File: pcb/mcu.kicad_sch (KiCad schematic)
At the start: 15 parts

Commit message: everything except crystal
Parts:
- added J?: Conn_02x07_Top_Bottom, symbol Connector_Generic:Conn_02x07_Top_Bottom
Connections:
- net +3.3V: now also J?.13 (Pin_13); no longer U?.G3 (VSS)
- net DONE: now also U?.D10 (PC8); no longer U?.E2 (PA5)
- net GND: now also U?.G3 (VSS), J?.14 (Pin_14)
- net PROGRAM_B: now also U?.D9 (PE7); no longer U?.E1 (PA6)
- net MCU_GPIO_1: now reaches U?.C1 (PA1)
- net MCU_GPIO_1: now also J?.1 (Pin_1)
- net MCU_GPIO_2: now reaches U?.C2 (PA0)
- net MCU_GPIO_2: now also J?.2 (Pin_2)
- net MCU_GPIO_3: now reaches U?.C3 (PE10)
- net MCU_GPIO_3: now also J?.3 (Pin_3)
- net MCU_GPIO_4: now reaches U?.C4 (PD13)
- net MCU_GPIO_4: now also J?.4 (Pin_4)
- net MCU_GPIO_5: now reaches U?.C5 (PD12)
- net MCU_GPIO_5: now also J?.5 (Pin_5)
- net MCU_GPIO_6: now reaches U?.C6 (PF9)
- net MCU_GPIO_6: now also J?.6 (Pin_6)
- net MCU_GPIO_12: now reaches U?.E10 (PE1)
- net MCU_GPIO_12: now also J?.12 (Pin_12)
- net MCU_GPIO_9: now reaches U?.E3 (PA4)
- net MCU_GPIO_9: now also J?.9 (Pin_9)
- net MCU_GPIO_10: now reaches U?.E4 (PB0)
- net MCU_GPIO_10: now also J?.10 (Pin_10)
- net MCU_GPIO_11: now reaches U?.E9 (PE0)
- net MCU_GPIO_11: now also J?.11 (Pin_11)
- new net MCU_GPIO_7: J?.7 (Pin_7), U?.E1 (PA6)
- new net MCU_GPIO_8: J?.8 (Pin_8), U?.E2 (PA5)
- no-connect marks 55 -> 43
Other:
- note added: "MCU PGIO HEADER"
- note added: "MCU clock out"
- moved on the sheet: C?

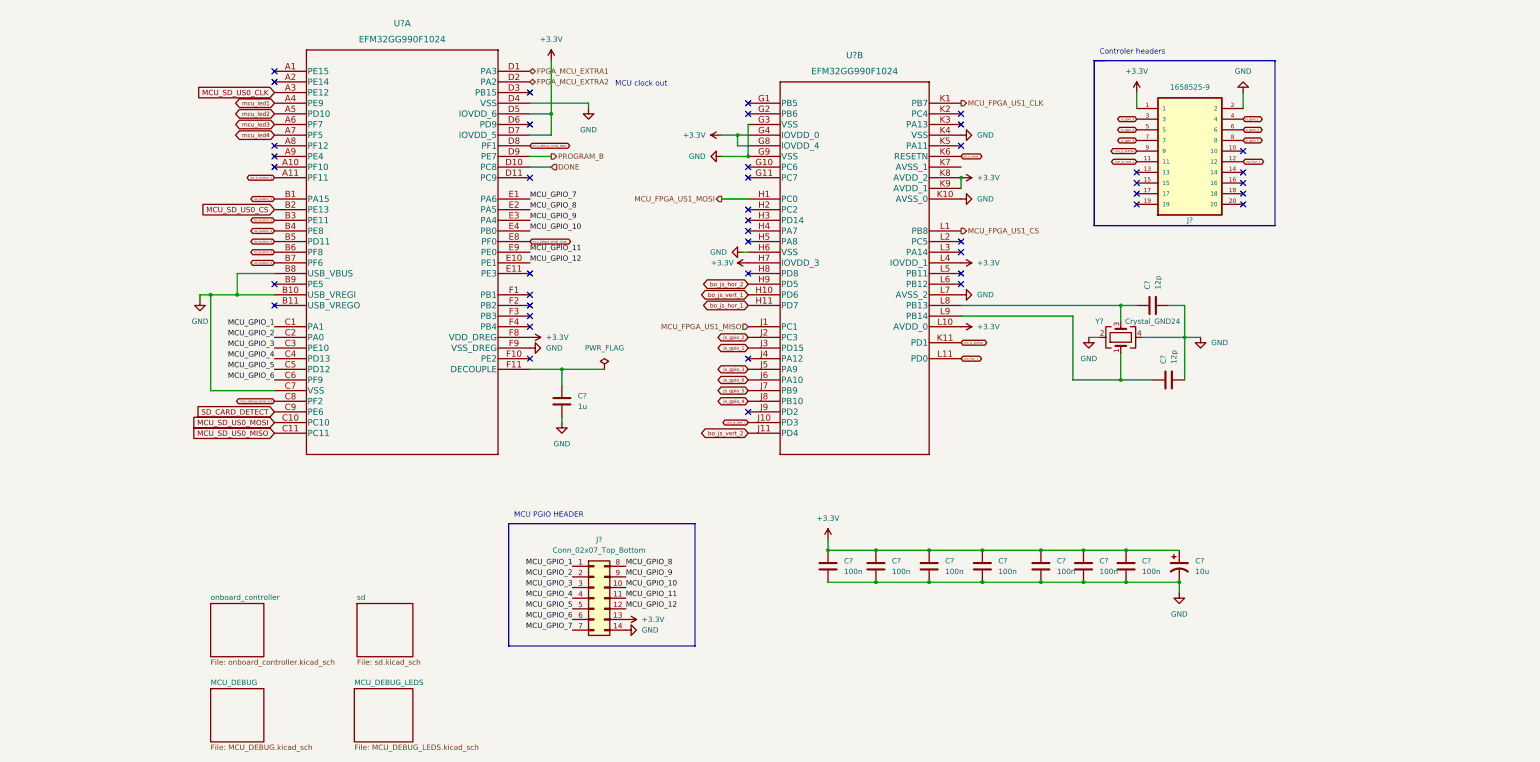
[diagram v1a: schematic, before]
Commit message: add oscilattor + spi debug+ cap on sramd
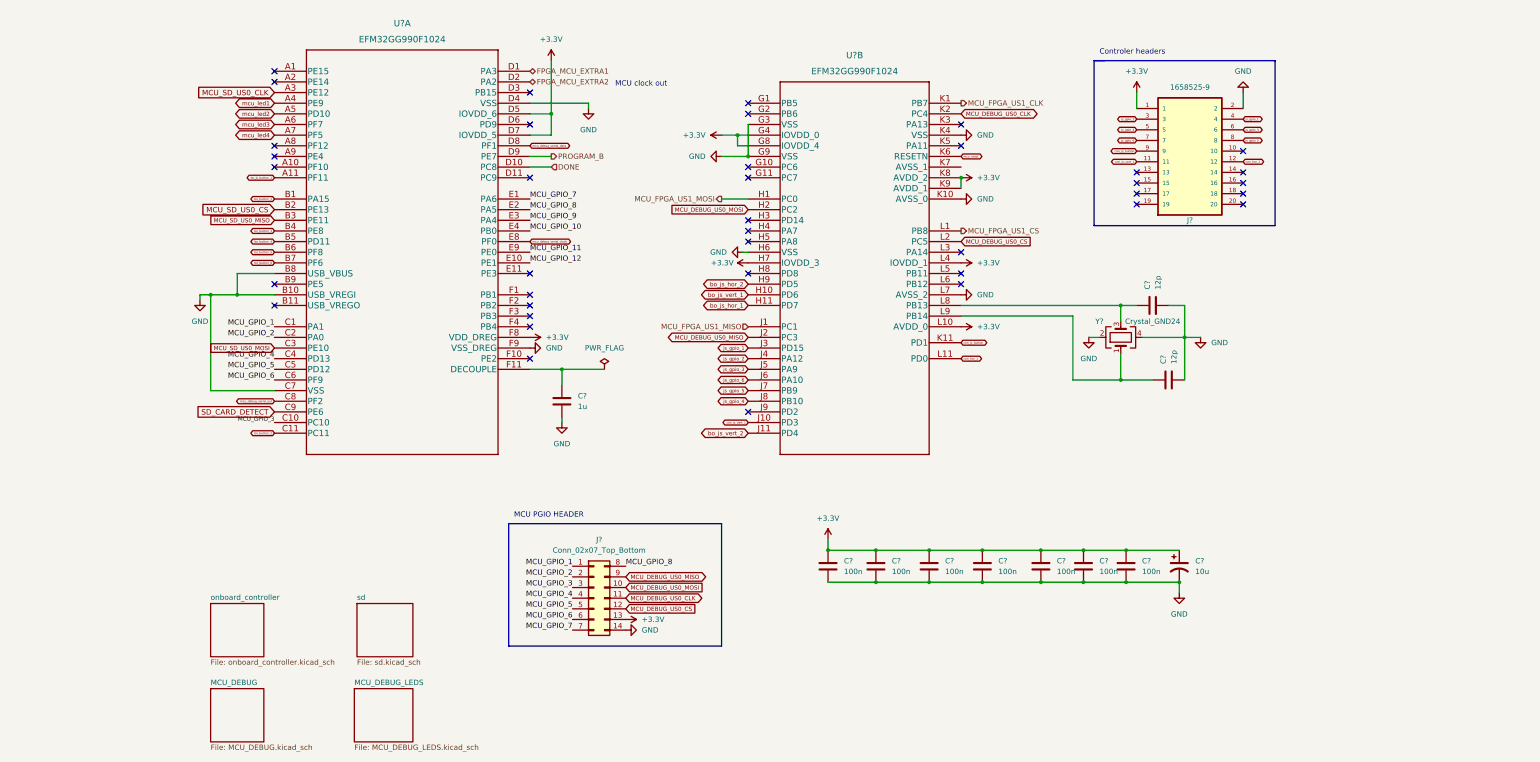
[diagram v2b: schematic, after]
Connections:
- net MCU_GPIO_10: no longer J?.10 (Pin_10)
- net MCU_GPIO_11: no longer J?.11 (Pin_11)
- net MCU_GPIO_12: no longer J?.12 (Pin_12)
- net MCU_GPIO_3: now also U?.C10 (PC10); no longer U?.C3 (PE10)
- net MCU_GPIO_9: no longer J?.9 (Pin_9)
- net MCU_SD_US0_MISO: now also U?.B3 (PE11); no longer U?.C11 (PC11)
- net MCU_SD_US0_MOSI: now also U?.C3 (PE10); no longer U?.C10 (PC10)
- net bo_button_2: now also U?.C11 (PC11); no longer U?.B3 (PE11)
- net js_gpio_2: now also U?.J4 (PA12); no longer U?.J2 (PC3)
- net MCU_DEBUG_US0_MOSI: now reaches U?.H2 (PC2)
- net MCU_DEBUG_US0_MOSI: now also J?.10 (Pin_10)
- net MCU_DEBUG_US0_CLK: now reaches U?.K2 (PC4)
- net MCU_DEBUG_US0_CLK: now also J?.11 (Pin_11)
- net MCU_DEBUG_US0_CS: now reaches U?.L2 (PC5)
- net MCU_DEBUG_US0_CS: now also J?.12 (Pin_12)
- new net MCU_DEBUG_US0_MISO: J?.9 (Pin_9), U?.J2 (PC3)
- no-connect marks 43 -> 39
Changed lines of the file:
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@@
   (no_connect (at 34.29 52.07))
   (no_connect (at 34.29 29.21))
-  (no_connect (at 147.32 62.23))
   (no_connect (at 198.12 72.39))
   (no_connect (at 95.25 97.79))
@@
   (no_connect (at 95.25 54.61))
   (no_connect (at 95.25 41.91))
-  (no_connect (at 147.32 97.79))
   (no_connect (at 147.32 64.77))
   (no_connect (at 147.32 77.47))
@@
   (no_connect (at 198.12 80.01))
   (no_connect (at 34.29 80.01))
-  (no_connect (at 198.12 39.37))
   (no_connect (at 198.12 41.91))
-  (no_connect (at 198.12 69.85))
   (no_connect (at 95.25 77.47))
   (no_connect (at 34.29 46.99))
@@
     (stroke (width 0) (type default) (color 0 0 0 0))
   )
-  (polyline (pts (xy 134.62 137.16) (xy 134.62 166.37))
-    (stroke (width 0) (type default) (color 0 0 0 0))
-  )
   (wire (pts (xy 236.22 102.87) (xy 243.84 102.87))
     (stroke (width 0) (type default) (color 0 0 0 0))
@@
     (stroke (width 0) (type default) (color 0 0 0 0))
   )
-  (polyline (pts (xy 134.62 166.37) (xy 90.17 166.37))
+  (polyline (pts (xy 134.62 137.16) (xy 140.97 137.16))
+    (stroke (width 0) (type default) (color 0 0 0 0))
+  )
+  (polyline (pts (xy 140.97 166.37) (xy 90.17 166.37))
     (stroke (width 0) (type default) (color 0 0 0 0))
   )
@@
     (stroke (width 0) (type default) (color 0 0 0 0))
   )
+  (polyline (pts (xy 140.97 137.16) (xy 140.97 166.37))
+    (stroke (width 0) (type default) (color 0 0 0 0))
+  )
   (wire (pts (xy 95.25 100.33) (xy 102.87 100.33))
     (stroke (width 0) (type default) (color 0 0 0 0))
@@
     (effects (font (size 1.27 1.27)) (justify right bottom))
   )
-  (label "MCU_GPIO_11" (at 118.11 154.94 0)
-    (effects (font (size 1.27 1.27)) (justify left bottom))
-  )
   (label "MCU_GPIO_5" (at 34.29 100.33 180)
     (effects (font (size 1.27 1.27)) (justify right bottom))
   )
-  (label "MCU_GPIO_3" (at 34.29 95.25 180)
-    (effects (font (size 1.27 1.27)) (justify right bottom))
+  (label "MCU_GPIO_3" (at 34.29 113.03 180)
+    (effects (font (size 1 1)) (justify right bottom))
   )
   (label "MCU_GPIO_6" (at 105.41 160.02 180)
@@
     (effects (font (size 1.27 1.27)) (justify right bottom))
   )
-  (label "MCU_GPIO_10" (at 118.11 152.4 0)
-    (effects (font (size 1.27 1.27)) (justify left bottom))
-  )
   (label "MCU_GPIO_6" (at 34.29 102.87 180)
     (effects (font (size 1.27 1.27)) (justify right bottom))
@@
     (effects (font (size 1.27 1.27)) (justify right bottom))
   )
-  (label "MCU_GPIO_12" (at 118.11 157.48 0)
-    (effects (font (size 1.27 1.27)) (justify left bottom))
-  )
   (label "MCU_GPIO_7" (at 105.41 162.56 180)
     (effects (font (size 1.27 1.27)) (justify right bottom))
@@
     (effects (font (size 1.27 1.27)) (justify left bottom))
   )
-  (label "MCU_GPIO_9" (at 118.11 149.86 0)
-    (effects (font (size 1.27 1.27)) (justify left bottom))
-  )
   (label "MCU_GPIO_1" (at 34.29 90.17 180)
     (effects (font (size 1.27 1.27)) (justify right bottom))
@@
   (label "MCU_GPIO_8" (at 118.11 147.32 0)
     (effects (font (size 1.27 1.27)) (justify left bottom))
+  )
+  (global_label "MCU_DEBUG_US0_CS" (shape input) (at 118.11 157.48 0) (fields_autoplaced)
+    (effects (font (size 1 1)) (justify left))
+    (property "Intersheet References" "${INTERSHEET_REFS}" (id 0) (at 135.3433 157.4175 0)
+      (effects (font (size 1 1)) (justify left) hide)
+    )
   )
   (global_label "mcu_led1" (shape bidirectional) (at 34.29 36.83 180) (fields_autoplaced)
@@
     )
   )
+  (global_label "MCU_DEBUG_US0_MOSI" (shape input) (at 118.11 152.4 0) (fields_autoplaced)
+    (effects (font (size 1 1)) (justify left))
+    (property "Intersheet References" "${INTERSHEET_REFS}" (id 0) (at 137.01 152.4625 0)
+      (effects (font (size 1 1)) (justify left) hide)
+    )
+  )
   (global_label "MCU_SD_US0_CLK" (shape input) (at 34.29 34.29 180) (fields_autoplaced)
     (effects (font (size 1.27 1.27)) (justify right))
@@
     )
   )
+  (global_label "js_gpio_2" (shape bidirectional) (at 147.32 97.79 180) (fields_autoplaced)
+    (effects (font (size 0.8 0.8)) (justify right))
+    (property "Intersheet References" "${INTERSHEET_REFS}" (id 0) (at 140.2381 97.74 0)
+      (effects (font (size 0.8 0.8)) (justify right) hide)
+    )
+  )
   (global_label "bo_js_button_1" (shape bidirectional) (at 34.29 54.61 180) (fields_autoplaced)
     (effects (font (size 0.5 0.5)) (justify right))
@@
     )
   )
+  (global_label "MCU_DEBUG_US0_CLK" (shape bidirectional) (at 118.11 154.94 0) (fields_autoplaced)
+    (effects (font (size 1 1)) (justify left))
+    (property "Intersheet References" "${INTERSHEET_REFS}" (id 0) (at 136.2005 154.8775 0)
+      (effects (font (size 1 1)) (justify left) hide)
+    )
+  )
+  (global_label "bo_button_2" (shape bidirectional) (at 34.29 115.57 180) (fields_autoplaced)
+    (effects (font (size 0.5 0.5)) (justify right))
+    (property "Intersheet References" "${INTERSHEET_REFS}" (id 0) (at 28.8162 115.5388 0)
+      (effects (font (size 0.5 0.5)) (justify right) hide)
+    )
+  )
   (global_label "bo_button_1" (shape bidirectional) (at 34.29 59.69 180) (fields_autoplaced)
     (effects (font (size 0.5 0.5)) (justify right))
@@
     (property "Intersheet References" "${INTERSHEET_REFS}" (id 0) (at 104.8667 46.9588 0)
       (effects (font (size 0.5 0.5)) (justify left) hide)
-    )
-  )
-  (global_label "MCU_SD_US0_MOSI" (shape input) (at 34.29 113.03 180) (fields_autoplaced)
-    (effects (font (size 1.27 1.27)) (justify right))
-    (property "Intersheet References" "${INTERSHEET_REFS}" (id 0) (at 14.0969 112.9506 0)
-      (effects (font (size 1.27 1.27)) (justify right) hide)
     )
   )
@@
     )
   )
+  (global_label "MCU_SD_US0_MOSI" (shape input) (at 34.29 95.25 180) (fields_autoplaced)
+    (effects (font (size 1 1)) (justify right))
+    (property "Intersheet References" "${INTERSHEET_REFS}" (id 0) (at 18.39 95.1875 0)
+      (effects (font (size 1 1)) (justify right) hide)
+    )
+  )
   (global_label "bo_button_3" (shape bidirectional) (at 34.29 67.31 180) (fields_autoplaced)
     (effects (font (size 0.5 0.5)) (justify right))
@@
     )
   )
+  (global_label "MCU_DEBUG_US0_CS" (shape input) (at 198.12 69.85 0) (fields_autoplaced)
+    (effects (font (size 1 1)) (justify left))
+    (property "Intersheet References" "${INTERSHEET_REFS}" (id 0) (at 215.3533 69.7875 0)
+      (effects (font (size 1 1)) (justify left) hide)
+    )
+  )
   (global_label "js_gpio_6" (shape bidirectional) (at 240.03 45.72 180) (fields_autoplaced)
     (effects (font (size 0.5 0.5)) (justify right))
@@
     )
   )
+  (global_label "MCU_DEBUG_US0_MISO" (shape bidirectional) (at 118.11 149.86 0) (fields_autoplaced)
+    (effects (font (size 1 1)) (justify left))
+    (property "Intersheet References" "${INTERSHEET_REFS}" (id 0) (at 137.01 149.9225 0)
+      (effects (font (size 1 1)) (justify left) hide)
+    )
+  )
   (global_label "mcu_led2" (shape bidirectional) (at 34.29 39.37 180) (fields_autoplaced)
     (effects (font (size 1 1)) (justify right))
@@
     )
   )
-  (global_label "MCU_SD_US0_MISO" (shape input) (at 34.29 115.57 180) (fields_autoplaced)
-    (effects (font (size 1.27 1.27)) (justify right))
-    (property "Intersheet References" "${INTERSHEET_REFS}" (id 0) (at 14.0969 115.4906 0)
-      (effects (font (size 1.27 1.27)) (justify right) hide)
-    )
-  )
   (global_label "js_gpio_5" (shape bidirectional) (at 265.43 45.72 0) (fields_autoplaced)
     (effects (font (size 0.5 0.5)) (justify left))
@@
     (property "Intersheet References" "${INTERSHEET_REFS}" (id 0) (at 28.8162 72.3588 0)
       (effects (font (size 0.5 0.5)) (justify right) hide)
-    )
-  )
-  (global_label "js_gpio_2" (shape bidirectional) (at 147.32 92.71 180) (fields_autoplaced)
-    (effects (font (size 0.8 0.8)) (justify right))
-    (property "Intersheet References" "${INTERSHEET_REFS}" (id 0) (at 140.2381 92.66 0)
-      (effects (font (size 0.8 0.8)) (justify right) hide)
     )
   )
@@
     )
   )
+  (global_label "MCU_DEBUG_US0_MISO" (shape bidirectional) (at 147.32 92.71 180) (fields_autoplaced)
+    (effects (font (size 1 1)) (justify right))
+    (property "Intersheet References" "${INTERSHEET_REFS}" (id 0) (at 128.42 92.6475 0)
+      (effects (font (size 1 1)) (justify right) hide)
+    )
+  )
+  (global_label "MCU_SD_US0_MISO" (shape input) (at 34.29 64.77 180) (fields_autoplaced)
+    (effects (font (size 1 1)) (justify right))
+    (property "Intersheet References" "${INTERSHEET_REFS}" (id 0) (at 18.39 64.7075 0)
+      (effects (font (size 1 1)) (justify right) hide)
+    )
+  )
   (global_label "js_gpio_4" (shape bidirectional) (at 147.32 107.95 180) (fields_autoplaced)
     (effects (font (size 0.8 0.8)) (justify right))
@@
     )
   )
-  (global_label "bo_button_2" (shape bidirectional) (at 34.29 64.77 180) (fields_autoplaced)
-    (effects (font (size 0.5 0.5)) (justify right))
-    (property "Intersheet References" "${INTERSHEET_REFS}" (id 0) (at 28.8162 64.7388 0)
-      (effects (font (size 0.5 0.5)) (justify right) hide)
+  (global_label "MCU_DEBUG_US0_CLK" (shape bidirectional) (at 198.12 39.37 0) (fields_autoplaced)
+    (effects (font (size 1 1)) (justify left))
+    (property "Intersheet References" "${INTERSHEET_REFS}" (id 0) (at 216.2105 39.3075 0)
+      (effects (font (size 1 1)) (justify left) hide)
     )
   )
@@
     )
   )
+  (global_label "MCU_DEBUG_US0_MOSI" (shape input) (at 147.32 62.23 180) (fields_autoplaced)
+    (effects (font (size 1 1)) (justify right))
+    (property "Intersheet References" "${INTERSHEET_REFS}" (id 0) (at 128.42 62.1675 0)
+      (effects (font (size 1 1)) (justify right) hide)
+    )
+  )

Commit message: add footprints
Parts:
- C301, C302, C303, C304, C305, C306, C307, C308, C311: renamed from C?; footprint (none) -> Capacitor_SMD:C_0805_2012Metric_Pad1.18x1.45mm_HandSolder
- C309, C310: renamed from C?; footprint (none) -> Capacitor_SMD:C_0603_1608Metric_Pad1.08x0.95mm_HandSolder
- gave numbers to parts that had none: 4
